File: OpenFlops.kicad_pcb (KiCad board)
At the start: 2 copper layers, 97 x 116 mm, 66 parts, among them J1 FDD, J2 USB_A_FEMALE, J3 PROG_PORT, J4 OLED, J5 OLED Mount, J6 OLED Mount, J7 SBAB_LOGO, J99 OSHW_LOGO, Q1 BSS138, Q2 BSS138, Q3 BSS138, Q4 BSS138, Q5 BSS138, Q6 BSS138, SW1 BT_RIGHT, SW2 BT_LEFT, U1 74HCT04, U2 STM32F105RBT6, U3 LM1117-3.3, Y1 8 MHz

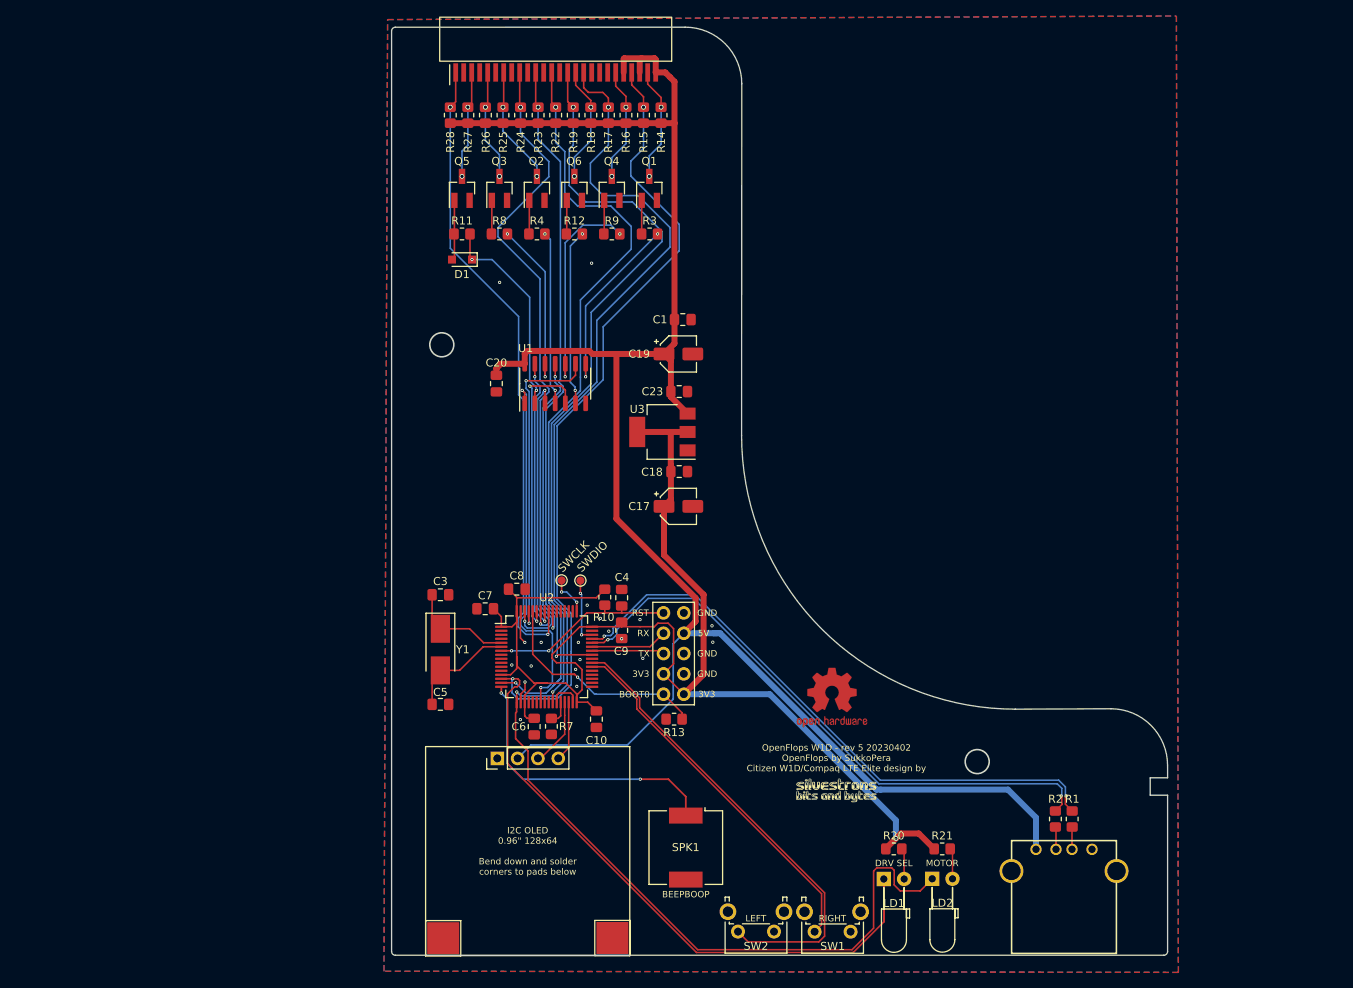
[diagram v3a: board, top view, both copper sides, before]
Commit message: rev 10; more smd for more assembly
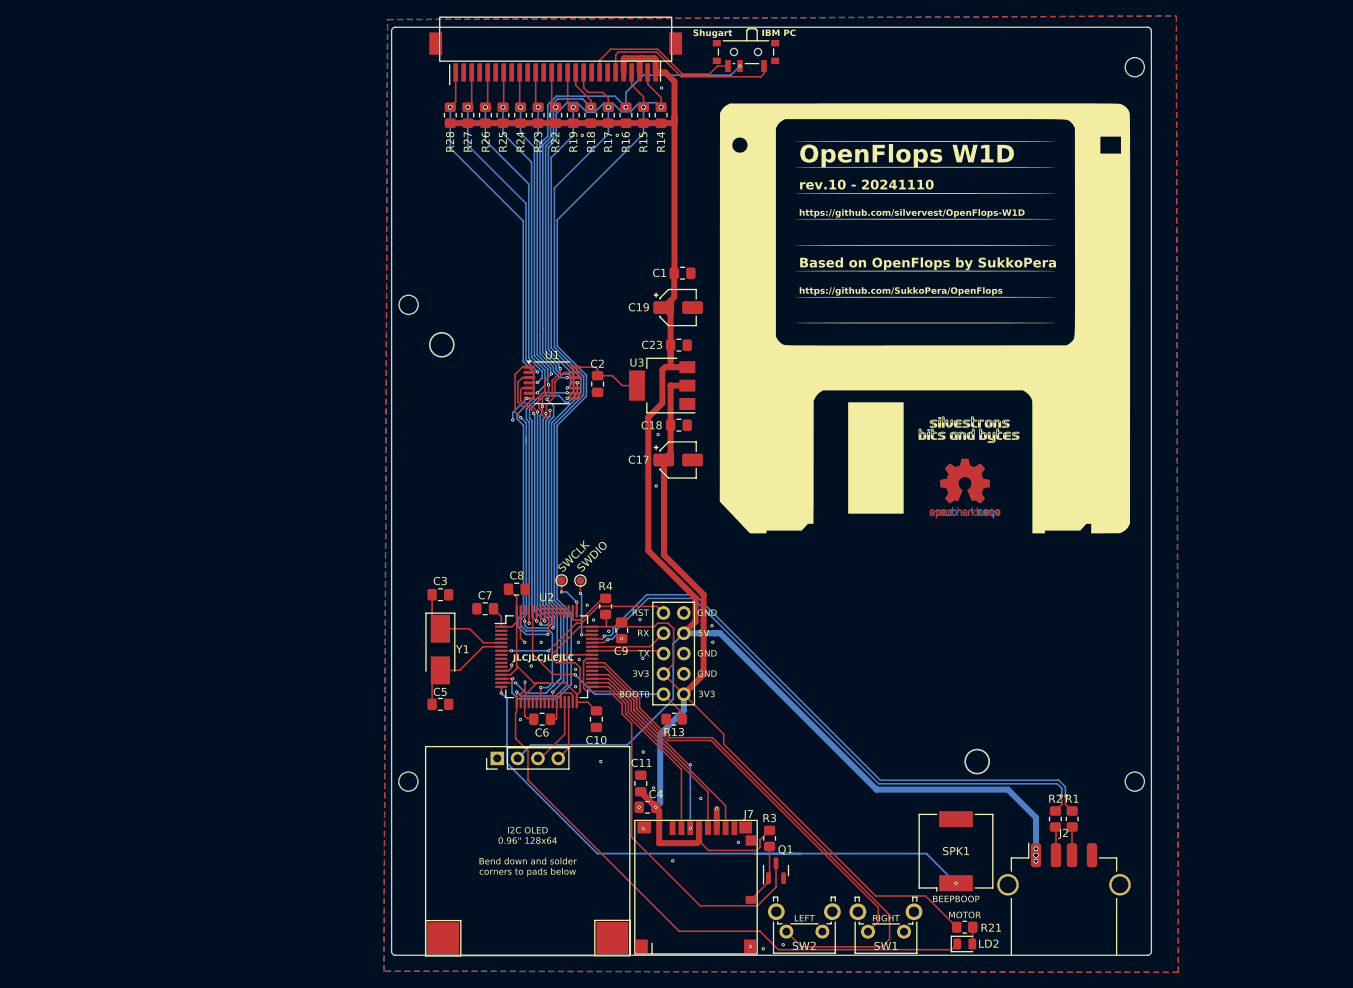
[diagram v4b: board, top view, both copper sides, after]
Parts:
- removed C20: 100n, Capacitor_SMD:C_0805_2012Metric_Pad1.18x1.45mm_HandSolder
- removed D1: 1N4148, Diode_SMD:D_SOD-323_HandSoldering
- removed LD1: LED_GREEN, LED_THT:LED_D3.0mm_Horizontal_O3.81mm_Z6.0mm
- removed Q2, Q3, Q4, Q5, Q6: BSS138, Package_TO_SOT_SMD:SOT-23_Handsoldering
- removed R10, R7: 4k7, Resistor_SMD:R_0805_2012Metric_Pad1.20x1.40mm_HandSolder
- removed R11, R12, R20, R8, R9: 1k, Resistor_SMD:R_0805_2012Metric_Pad1.20x1.40mm_HandSolder
- added C11: 100n, Capacitor_SMD:C_0805_2012Metric_Pad1.18x1.45mm_HandSolder, F.Cu at (141.6, 130.1)
- added C2: 100n, Capacitor_SMD:C_0805_2012Metric_Pad1.18x1.45mm_HandSolder, F.Cu at (136.2, 80.2)
- added G***: LOGO, Silvestron Components:sbab-text-logo-tiny, F.Cu at (182.4, 86.0)
- added G***: LOGO, LOGO, F.Cu at (177.1, 72.0)
- added G***: LOGO, LOGO, B.Cu at (177.1, 72.0)
- added G***: LOGO, Silvestron Components:sbab-text-logo-tiny, B.Cu at (182.9, 86.0)
- added J99: OSHW_LOGO, Symbol:OSHW-Logo2_9.8x8mm_Copper, B.Cu at (182.1, 93.3)
- added REF**: W1D screw mount, Silvestron Components:W1D screw mount, F.Cu at (116.5, 70.3)
- added REF**: W1D screw mount, Silvestron Components:W1D screw mount, F.Cu at (207.3, 129.9)
- added REF**: W1D screw mount, Silvestron Components:W1D screw mount, F.Cu at (116.5, 129.9)
- added REF**: W1D screw mount, Silvestron Components:W1D screw mount, F.Cu at (207.3, 40.6)
- added SW3: CHG/RDY, Button_Switch_SMD:SW_SPDT_PCM12, F.Cu at (154.8, 39.0)
- C4: value 100n -> 10u
- J2: footprint OpenFlops:USB_A_FEMALE -> Connector_USB:USB_A_Receptacle_GCT_USB1046
- J7: value SBAB_LOGO -> Micro_SD_Card_Det1; footprint Silvestron Components:sbab-tiny-logo -> Silvestron Components:microSD_XUNPU_TF-114
- LD2: value LED_RED -> LED_GREEN; footprint LED_THT:LED_D3.0mm_Horizontal_O3.81mm_Z6.0mm -> LED_SMD:LED_0805_2012Metric
- Q1: value BSS138 -> 2N7002; footprint Package_TO_SOT_SMD:SOT-23_Handsoldering -> Package_TO_SOT_SMD:SOT-23
- R13: value 4k7 -> 10k
- R3: value 1k -> 10k
- U1: value 74HCT04 -> SN74LVC07A; footprint Package_SO:SOIC-14_3.9x8.7mm_P1.27mm -> Package_SO:TSSOP-14_4.4x5mm_P0.65mm
- moved Q1 86.8 mm to (158.5, 141.0)
- moved R3 77.0 mm to (157.7, 137.0), turned to -90 degrees
- moved R4 47.3 mm to (137.2, 108.0), turned to 90 degrees
- moved SPK1 33.8 mm to (181.0, 138.6), turned to 90 degrees
- moved J99 31.0 mm to (182.1, 93.3)
- moved C4 26.4 mm to (142.4, 133.1), turned to 180 degrees
- moved J7 21.5 mm to (148.3, 143.2)
- moved R21 10.2 mm to (182.1, 148.1)
- moved LD2 9.11 mm to (182.1, 150.2)
- moved SW1 6.68 mm to (174.5, 148.7)
- moved SW2 6.05 mm to (164.3, 148.7)
- moved C1 5.80 mm to (146.8, 66.3)
- moved C18 5.80 mm to (146.4, 85.3)
- moved C23 5.80 mm to (146.4, 75.3)
- moved C17 5.80 mm to (146.3, 89.7)
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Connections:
- C4 pad 1: /nrst -> +3V3
- J1 pad 13: unconnected-(J1-Pad13) -> GND
- J1 pad 8: unconnected-(J1-Pad8) -> /~{rdy}
- J1 pad 9: unconnected-(J1-Pad9) -> GND
- Q1 pad 1: Net-(Q1-Pad1) -> /sd_det
- Q1 pad 3: /~{index} -> /card_det
- R16 pad 2: /~{dskchg} -> /~{dskchg/rdy}
- R3 pad 1: Net-(Q1-Pad1) -> +3V3
- R3 pad 2: Net-(R3-Pad2) -> /sd_det
- R4 pad 1: Net-(Q2-Pad1) -> +3V3
- R4 pad 2: Net-(R4-Pad2) -> /~{mtron}
- U1 pad 10: Net-(R9-Pad2) -> /~{redwc}
- U1 pad 11: /~{dskchg_3v3} -> /~{redwc_3v3}
- U1 pad 12: Net-(R8-Pad2) -> /~{dskchg/rdy}
- U1 pad 13: /~{wprot_3v3} -> /~{dskchg_3v3}
- U1 pad 14: +5V -> +3V3
- U1 pad 2: Net-(D1-Pad1) -> /~{rdata}
- U1 pad 3: /~{trk0_3v3} -> /~{wprot_3v3}
- U1 pad 4: Net-(R4-Pad2) -> /~{wpt}
- U1 pad 5: /~{redwc_3v3} -> /~{trk0_3v3}
- U1 pad 6: Net-(R12-Pad2) -> /~{trk00}
- U1 pad 8: Net-(R3-Pad2) -> /~{index}
- U2 pad 28: /boot1 -> GND
- U2 pad 40: unconnected-(U2-Pad40) -> /card_det
- U2 pad 53: GND -> unconnected-(U2-PC12-Pad53)
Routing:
- net /~{drvs}: track 180.3 -> 97.1 mm
- net /~{dskchg/rdy}: track 0.00 -> 65.7 mm, vias 0 -> 3
- net /card_det: track 0.00 -> 52.9 mm
- net /~{index}: track 14.3 -> 59.5 mm
- net +3V3: track 172.8 -> 215.4 mm
- net /jb: track 36.3 -> 78.1 mm
- net /~{redwc}: track 14.6 -> 49.8 mm
- net /~{wpt}: track 13.8 -> 43.1 mm
- net /~{trk00}: track 14.8 -> 43.7 mm
- net /~{rdata}: track 13.5 -> 42.3 mm
- net /spi_do: track 0.00 -> 26.8 mm
- net Net-(R9-Pad2): track 26.6 -> 0.00 mm, vias 2 -> 0
- net Net-(D1-Pad1): track 26.2 -> 0.00 mm, vias 2 -> 0
- net +5V: track 235.9 -> 209.9 mm, vias 0 -> 4
- net /spi_di: track 0.00 -> 25.6 mm, vias 0 -> 2
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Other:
- board size 97 x 116 mm -> 95 x 116 mm
- board text added: "Based on OpenFlops by SukkoPera"
- board text added: "IBM PC"
- board text added: "JLCJLCJLCJLC"
- board text added: "OpenFlops W1D"
- board text added: "Shugart"
- board text added: "There's a lot of {dblquote}wasted{dblquote} space back here, so I wanted to just write a little note to you, the person using this product. It's just a short note to say that I appreciate you, and the community around you, that help restore, maintain, and remember these old and beautiful machines. Without people like you, the machine this goes in would probably have been destined for the landfill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"
- board text added: "https://github.com/SukkoPera/OpenFlops"
- board text added: "https://github.com/silvervest/OpenFlops-W1D"
- board text added: "rev.10 - 20241110"
- board text removed: "DRV SEL"
- board text removed: "OpenFlops W1D - rev 5 20230402 OpenFlops by SukkoPera Citizen W1D/Compaq LTE Elite design by"

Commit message: rev 11; fixed issue with usb port being too far forward
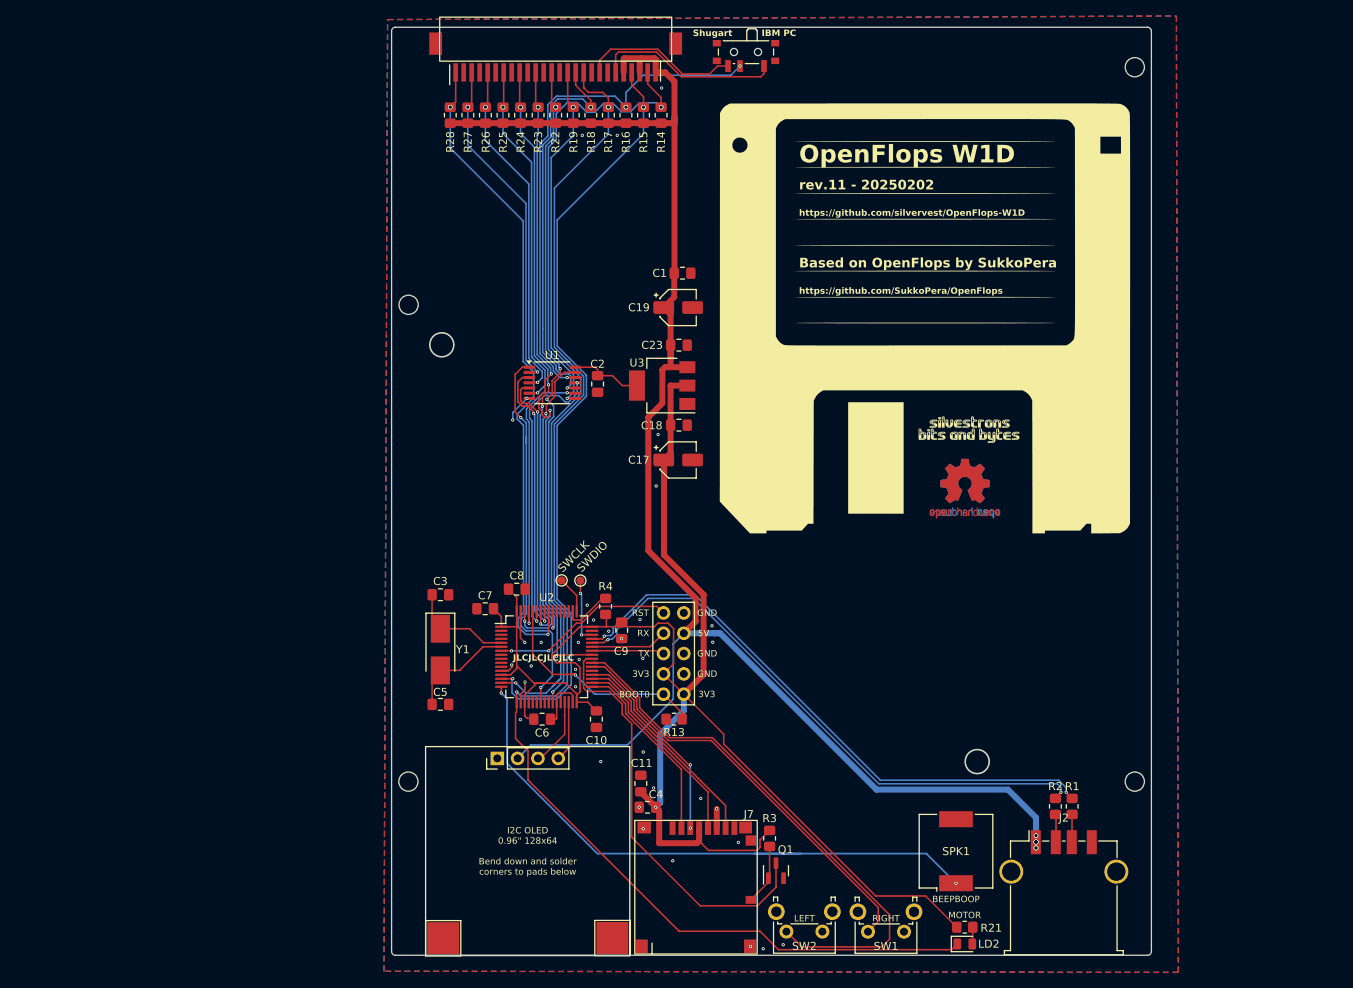
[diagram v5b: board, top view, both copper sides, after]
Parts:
- J2: footprint Connector_USB:USB_A_Receptacle_GCT_USB1046 -> Connector_USB:USB_A_TE_292303-7_Horizontal
- moved J2 2.50 mm to (194.5, 143.9)
- moved R1 1.57 mm to (195.5, 133.0)
- moved R2 1.57 mm to (193.4, 133.0)
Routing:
- net /usb-: track 74.5 -> 72.9 mm
- net +5V: track 209.9 -> 208.3 mm
- net /usb+: track 75.3 -> 73.8 mm
- net /usb-r: track 3.56 -> 3.02 mm
- net /usb+r: track 3.54 -> 3.00 mm
- net /swclk: track 5.03 -> 4.65 mm, vias 2 -> 0
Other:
- board text added: "rev.11 - 20250202"
- board text removed: "rev.10 - 20241110"
